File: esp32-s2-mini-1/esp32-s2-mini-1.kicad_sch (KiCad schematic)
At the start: 17 parts, among them J1 Conn_01x04_Male, J2 USB_C_Receptacle_USB2.0, U1 ESP32-S2-MINI-1-N4, U2 LM1117-3.3

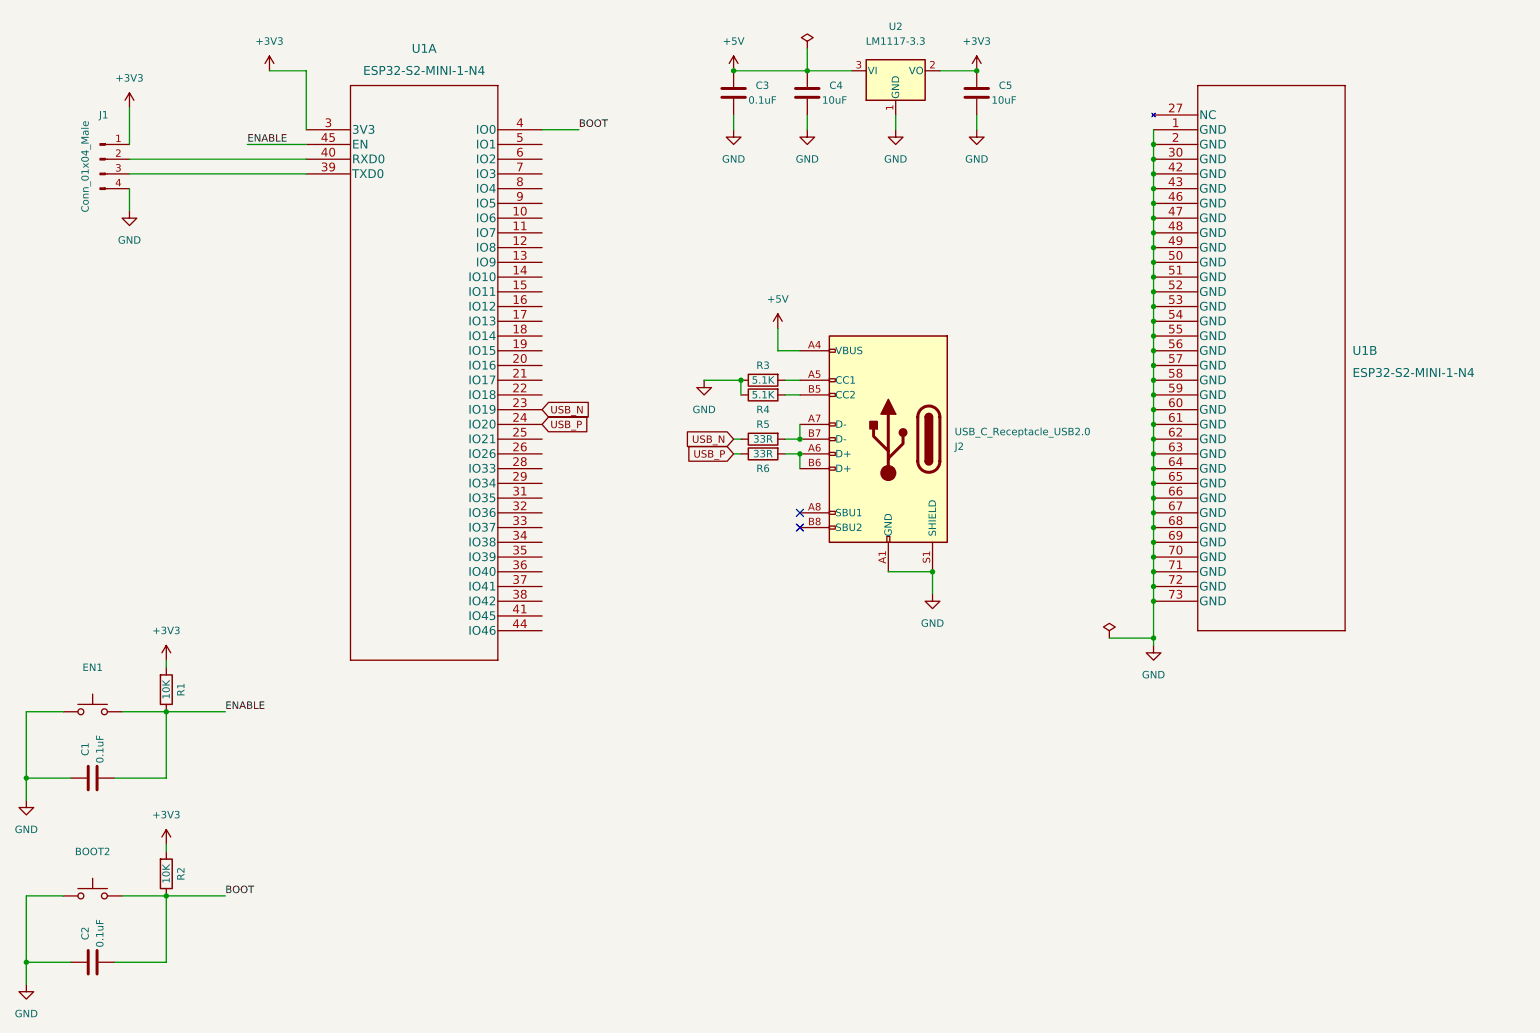
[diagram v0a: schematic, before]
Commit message: Seems some labels were missing from original saves
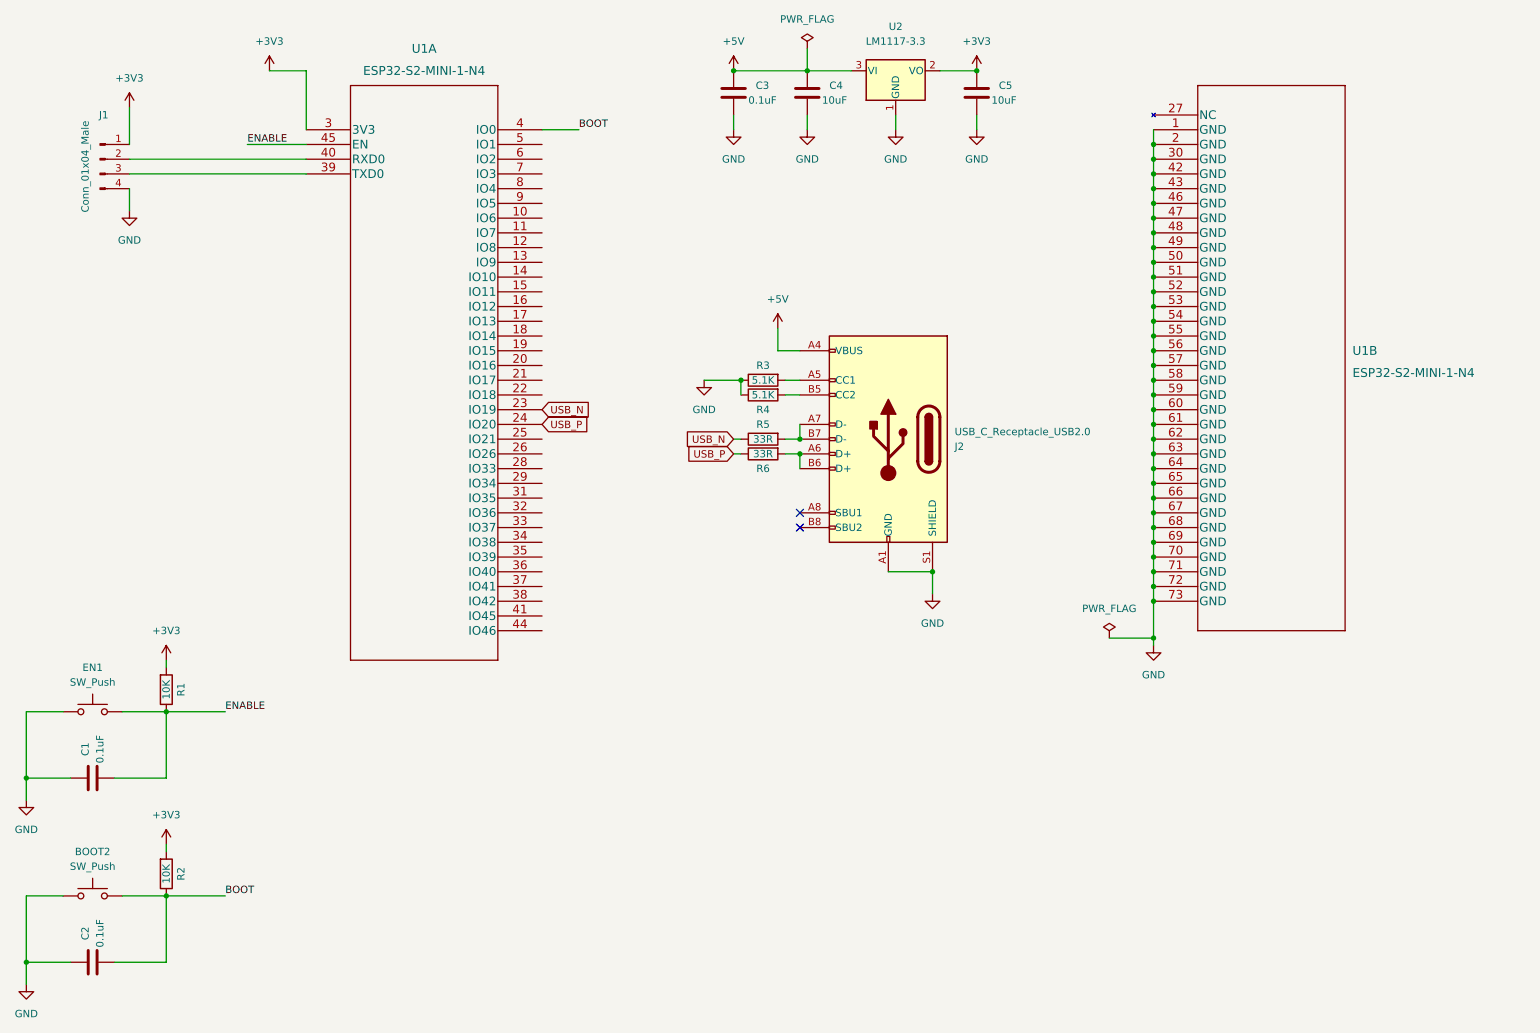
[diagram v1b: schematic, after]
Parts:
- BOOT2, EN1: value (none) -> SW_Push; footprint (none) -> Button_Switch_SMD:SW_SPST_Panasonic_EVQPL_3PL_5PL_PT_A08
- J1: footprint (none) -> Connector_PinHeader_2.54mm:PinHeader_1x04_P2.54mm_Vertical
- J2: footprint (none) -> USB-C-Power-tester:TYPE-C-31-M-12
- U1: footprint (none) -> footprints_esp:ESP32-S2-MINI-1-N4
- U2: footprint (none) -> Package_TO_SOT_SMD:SOT-223
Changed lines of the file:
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@@
     (property "Reference" "U2" (id 0) (at 175.26 20.32 0))
     (property "Value" "LM1117-3.3" (id 1) (at 175.26 22.86 0))
-    (property "Footprint" "" (id 2) (at 175.26 27.94 0)
+    (property "Footprint" "Package_TO_SOT_SMD:SOT-223" (id 2) (at 175.26 27.94 0)
       (effects (font (size 1.27 1.27)) hide)
     )
@@
     (property "Reference" "J1" (id 0) (at 38.735 35.56 0))
     (property "Value" "Conn_01x04_Male" (id 1) (at 35.56 44.45 90))
-    (property "Footprint" "" (id 2) (at 38.1 43.18 0)
+    (property "Footprint" "Connector_PinHeader_2.54mm:PinHeader_1x04_P2.54mm_Vertical" (id 2) (at 38.1 43.18 0)
       (effects (font (size 1.27 1.27)) hide)
     )
@@
     (in_bom yes) (on_board yes) (fields_autoplaced)
     (property "Reference" "BOOT2" (id 0) (at 36.83 162.56 0))
-    (property "Value" "" (id 1) (at 36.83 165.1 0))
-    (property "Footprint" "" (id 2) (at 36.83 165.1 0)
+    (property "Value" "SW_Push" (id 1) (at 36.83 165.1 0))
+    (property "Footprint" "Button_Switch_SMD:SW_SPST_Panasonic_EVQPL_3PL_5PL_PT_A08" (id 2) (at 36.83 165.1 0)
       (effects (font (size 1.27 1.27)) hide)
     )
@@
       (effects (font (size 1.524 1.524)) (justify left))
     )
-    (property "Footprint" "" (id 2) (at 240.03 26.924 0)
+    (property "Footprint" "footprints_esp:ESP32-S2-MINI-1-N4" (id 2) (at 240.03 26.924 0)
       (effects (font (size 1.524 1.524)) hide)
     )
@@
     (in_bom yes) (on_board yes) (fields_autoplaced)
     (property "Reference" "EN1" (id 0) (at 36.83 130.81 0))
-    (property "Value" "" (id 1) (at 36.83 133.35 0))
-    (property "Footprint" "" (id 2) (at 36.83 133.35 0)
+    (property "Value" "SW_Push" (id 1) (at 36.83 133.35 0))
+    (property "Footprint" "Button_Switch_SMD:SW_SPST_Panasonic_EVQPL_3PL_5PL_PT_A08" (id 2) (at 36.83 133.35 0)
       (effects (font (size 1.27 1.27)) hide)
     )
@@
       (effects (font (size 1.27 1.27)) (justify right))
     )
-    (property "Footprint" "" (id 2) (at 170.18 91.44 0)
+    (property "Footprint" "USB-C-Power-tester:TYPE-C-31-M-12" (id 2) (at 170.18 91.44 0)
       (effects (font (size 1.27 1.27)) hide)
     )
@@
       (effects (font (size 1.524 1.524)))
     )
-    (property "Footprint" "" (id 2) (at 93.98 29.464 0)
+    (property "Footprint" "footprints_esp:ESP32-S2-MINI-1-N4" (id 2) (at 93.98 29.464 0)
       (effects (font (size 1.524 1.524)) hide)
     )
@@
       (effects (font (size 1.27 1.27)) hide)
     )
-    (property "Value" "" (id 1) (at 212.09 120.65 0))
+    (property "Value" "PWR_FLAG" (id 1) (at 212.09 120.65 0))
     (property "Footprint" "" (id 2) (at 212.09 125.73 0)
       (effects (font (size 1.27 1.27)) hide)
@@
       (effects (font (size 1.27 1.27)) hide)
     )
-    (property "Value" "" (id 1) (at 160.02 19.05 0))
+    (property "Value" "PWR_FLAG" (id 1) (at 160.02 19.05 0))
     (property "Footprint" "" (id 2) (at 160.02 24.13 0)
       (effects (font (size 1.27 1.27)) hide)

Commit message: The basic structure of the pcb is ready. Pins are unconnected, and extra components are missing still.
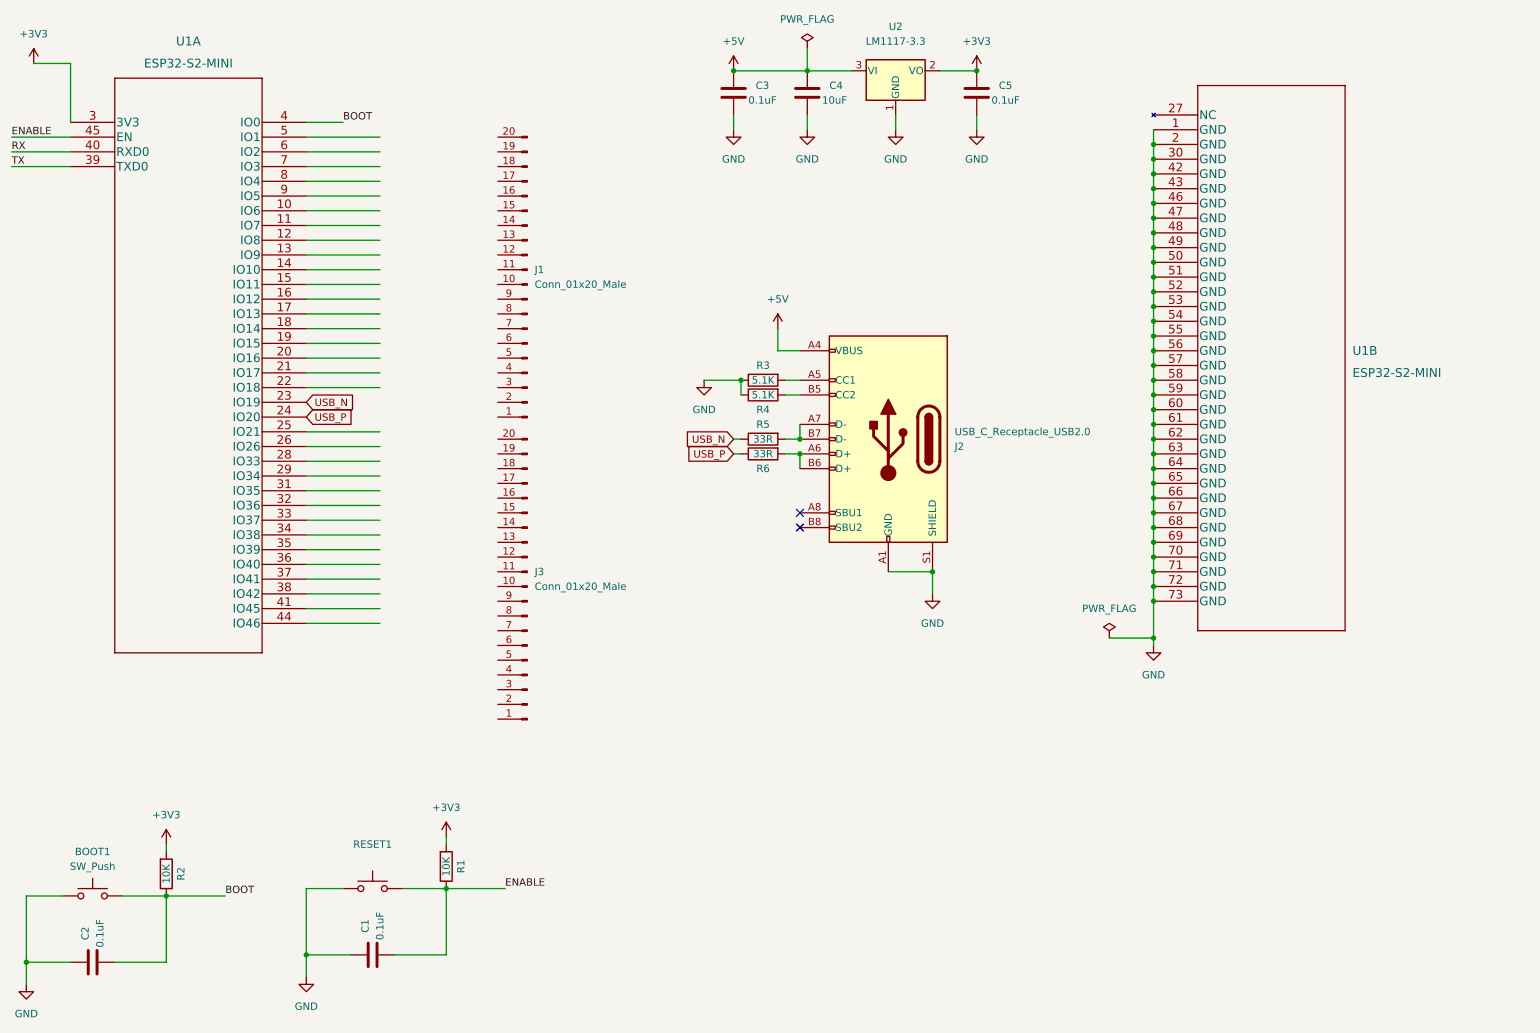
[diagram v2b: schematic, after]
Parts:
- removed J1: Conn_01x04_Male, Connector_PinHeader_2.54mm:PinHeader_1x04_P2.54mm_Vertical, symbol Connector:Conn_01x04_Male
- added J1, J3: Conn_01x20_Male, Connector_PinHeader_2.54mm:PinHeader_1x20_P2.54mm_Vertical, symbol Connector:Conn_01x20_Male
- C5: value 10uF -> 0.1uF; footprint Capacitor_SMD:C_0805_2012Metric -> Capacitor_SMD:C_0603_1608Metric
- RESET1: renamed from EN1; value SW_Push -> (none); footprint Button_Switch_SMD:SW_SPST_Panasonic_EVQPL_3PL_5PL_PT_A08 -> (none)
- U1: value ESP32-S2-MINI-1-N4 -> ESP32-S2-MINI
- renumbered BOOT2 to BOOT1
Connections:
- net RX: now reaches U1.40 (RXD0)
- net TX: now reaches U1.39 (TXD0)
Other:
- moved on the sheet: C1, R1, RESET1, U1A
